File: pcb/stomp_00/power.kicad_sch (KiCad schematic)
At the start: 10 parts, among them J17 9V_Power_Input, U11 AP7333-33SRG, U8 XL1509-5.0

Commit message: came back to the project
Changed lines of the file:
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@@
+    (effects (font (size 1.27 1.27)) (justify left top))
+  )
+  (text_box "9V DC input goes to 5V via XL1509-5.0 switching regulator. AP7333 (or maybe AP7313, lower noise, used in Teensy audio adaptor schematic) provides clean 3.3V to SGTL5000."
+    (at 69.85 13.97 0) (size 60.96 30.48)
+    (stroke (width 0) (type default))
+    (fill (type none))
     (effects (font (size 1.27 1.27)) (justify left top))
   )

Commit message: seeing whether everything will fit...
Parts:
- J17: footprint Connector_BarrelJack:BarrelJack_Horizontal -> Connector_PinHeader_2.54mm:PinHeader_1x03_P2.54mm_Vertical
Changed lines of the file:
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@@
       (effects (font (size 1.27 1.27)))
     )
-    (property "Footprint" "Connector_BarrelJack:BarrelJack_Horizontal" (at 48.26 34.544 0)
+    (property "Footprint" "Connector_PinHeader_2.54mm:PinHeader_1x03_P2.54mm_Vertical" (at 48.26 34.544 0)
       (effects (font (size 1.27 1.27)) hide)
     )

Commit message: pcb...
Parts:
- removed C5, C8: 1uF, Capacitor_SMD:C_0603_1608Metric, symbol Device:C
- removed U11: AP7333-33SRG, Package_TO_SOT_SMD:SOT-23, symbol Regulator_Linear:SPX2920M3-3.3_SOT223
- C27: value 180uF 35V -> 470uF 25V
- L1: value 68uH/2A -> 22uH/2A
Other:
- note removed: "Voltage regulator for DAC, provides low-noise signal. AP7333-33SRG, as used by Pimoroni. Cheap and available on JLCPCB. Possible alternative is MIC5219-3.3YM5."

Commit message: tweaking layout, issue with usb socket placement
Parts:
- C27: footprint Capacitor_THT:CP_Radial_D8.0mm_P3.50mm -> Capacitor_THT:CP_Radial_D10.0mm_P5.00mm
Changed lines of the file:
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@@
       (effects (font (size 1.27 1.27)) (justify left))
     )
-    (property "Footprint" "Capacitor_THT:CP_Radial_D8.0mm_P3.50mm" (at 103.378 63.246 0)
+    (property "Footprint" "Capacitor_THT:CP_Radial_D10.0mm_P5.00mm" (at 103.378 63.246 0)
       (effects (font (size 1.27 1.27)) hide)
     )

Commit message: 9v power stuff
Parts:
- removed J17: 9V_Power_Input, Connector_PinHeader_2.54mm:PinHeader_1x03_P2.54mm_Vertical, symbol Connector:Barrel_Jack_Switch
- added J8: Barrel_Jack, symbol Connector:Barrel_Jack
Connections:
- net +9V: now also J8.1
- net GND: now also J8.2
- no-connect marks 1 -> 0
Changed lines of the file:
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@@
   (junction (at 40.513 59.436) (diameter 0) (color 0 0 0 0)
   )
-  (no_connect (at 54.61 35.56))
   (wire (pts (xy 40.513 59.436) (xy 48.133 59.436))
     (stroke (width 0) (type default))
@@
     (fill (type none))
     (effects (font (size 1.27 1.27)) (justify left top))
-  )
-  (symbol (lib_id "Connector:Barrel_Jack_Switch") (at 46.99 35.56 0) (mirror x) (unit 1)
-    (in_bom yes) (on_board yes) (dnp no)
-    (property "Reference" "J17" (at 46.99 42.3799 0)
-      (effects (font (size 1.27 1.27)))
-    )
-    (property "Value" "9V_Power_Input" (at 46.99 40.4589 0)
-      (effects (font (size 1.27 1.27)))
-    )
-    (property "Footprint" "Connector_PinHeader_2.54mm:PinHeader_1x03_P2.54mm_Vertical" (at 48.26 34.544 0)
-      (effects (font (size 1.27 1.27)) hide)
-    )
-    (property "Datasheet" "~" (at 48.26 34.544 0)
-      (effects (font (size 1.27 1.27)) hide)
-    )
-    (pin "1")
-    (pin "2")
-    (pin "3")
-    (instances
-      (project "dk2_00"
-        (path "/87a59a99-d509-467e-85da-26d34072acb7/be1ddc4d-f499-4b75-b4b5-b626a320d90d"
-          (reference "J17") (unit 1)
-        )
-      )
-      (project "stomp_00"
-        (path "/8f4a2eb0-078b-46cb-b534-a4acd11d130e"
-          (reference "J4") (unit 1)
-        )
-        (path "/8f4a2eb0-078b-46cb-b534-a4acd11d130e/72df8ca6-692f-47f3-a8bd-ce94f6cd776a"
-          (reference "J1") (unit 1)
-        )
-        (path "/8f4a2eb0-078b-46cb-b534-a4acd11d130e/9942492d-ba8b-45b2-b427-7fe14bedb7e0"
-          (reference "J4") (unit 1)
-        )
-      )
-    )
   )
   (symbol (lib_id "Regulator_Switching:XL1509-5.0") (at 68.453 61.976 0) (unit 1)
@@
         )
       )
+    )
+  )
+  (symbol (lib_id "Connector:Barrel_Jack") (at 46.99 35.56 0) (unit 1)
+    (in_bom yes) (on_board yes) (dnp no) (fields_autoplaced)
+    (property "Reference" "J8" (at 46.99 28.7401 0)
+      (effects (font (size 1.27 1.27)))
+    )
+    (property "Value" "Barrel_Jack" (at 46.99 30.6611 0)
+      (effects (font (size 1.27 1.27)))
+    )
+    (property "Footprint" "" (at 48.26 36.576 0)
+      (effects (font (size 1.27 1.27)) hide)
+    )
+    (property "Datasheet" "~" (at 48.26 36.576 0)
+      (effects (font (size 1.27 1.27)) hide)
+    )
+    (pin "1")
+    (pin "2")
+    (instances
+      (project "stomp_00"
+        (path "/8f4a2eb0-078b-46cb-b534-a4acd11d130e/72df8ca6-692f-47f3-a8bd-ce94f6cd776a"
+          (reference "J8") (unit 1)
+        )
+      )

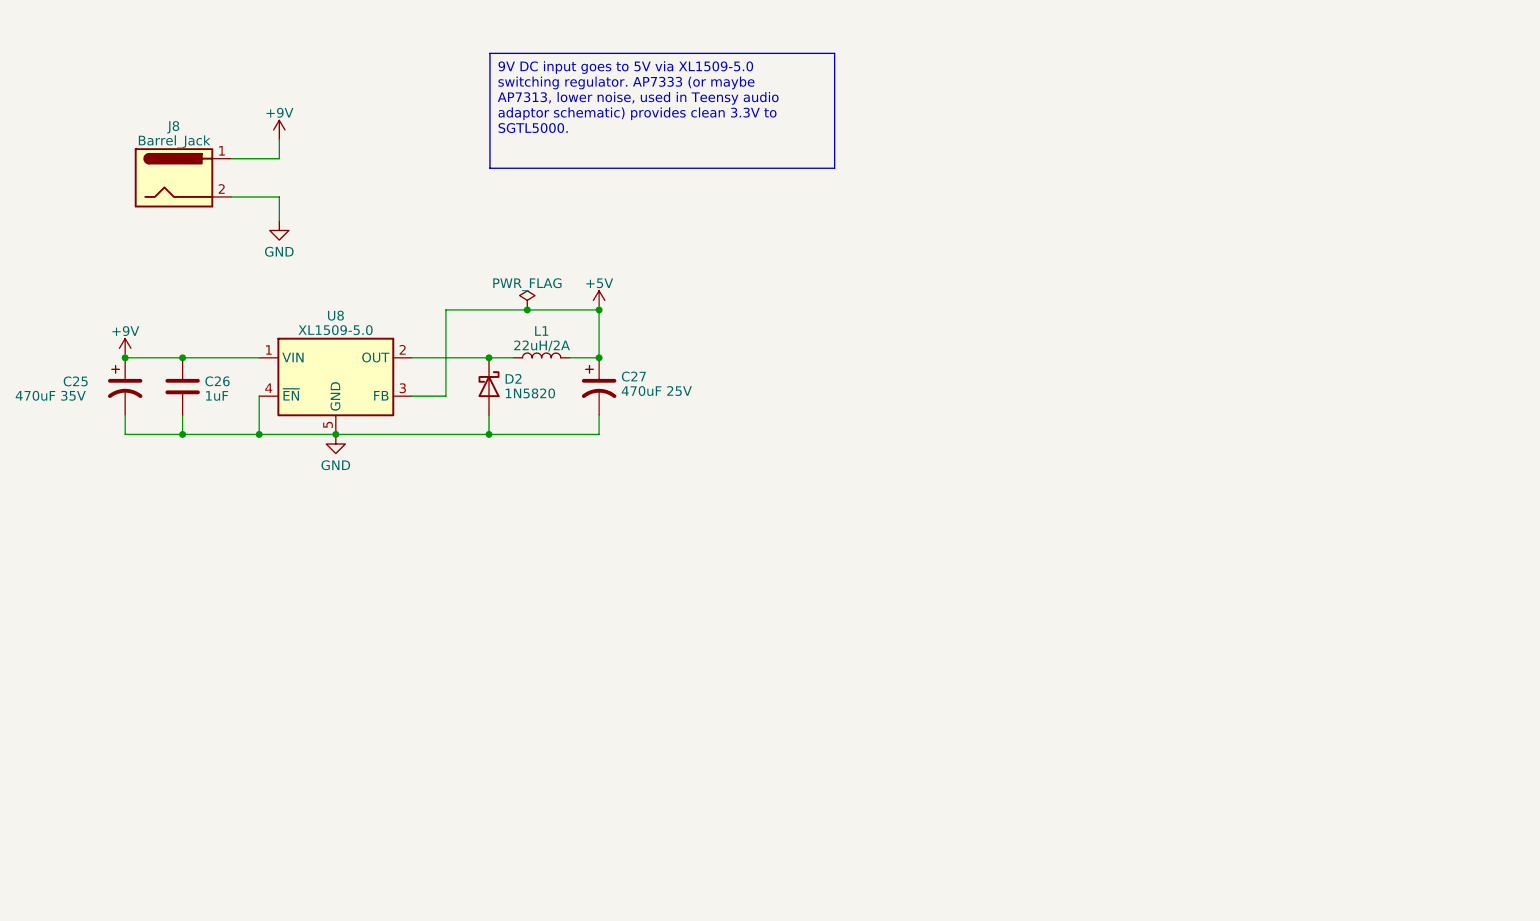
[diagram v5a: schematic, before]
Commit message: changed voltage regulator
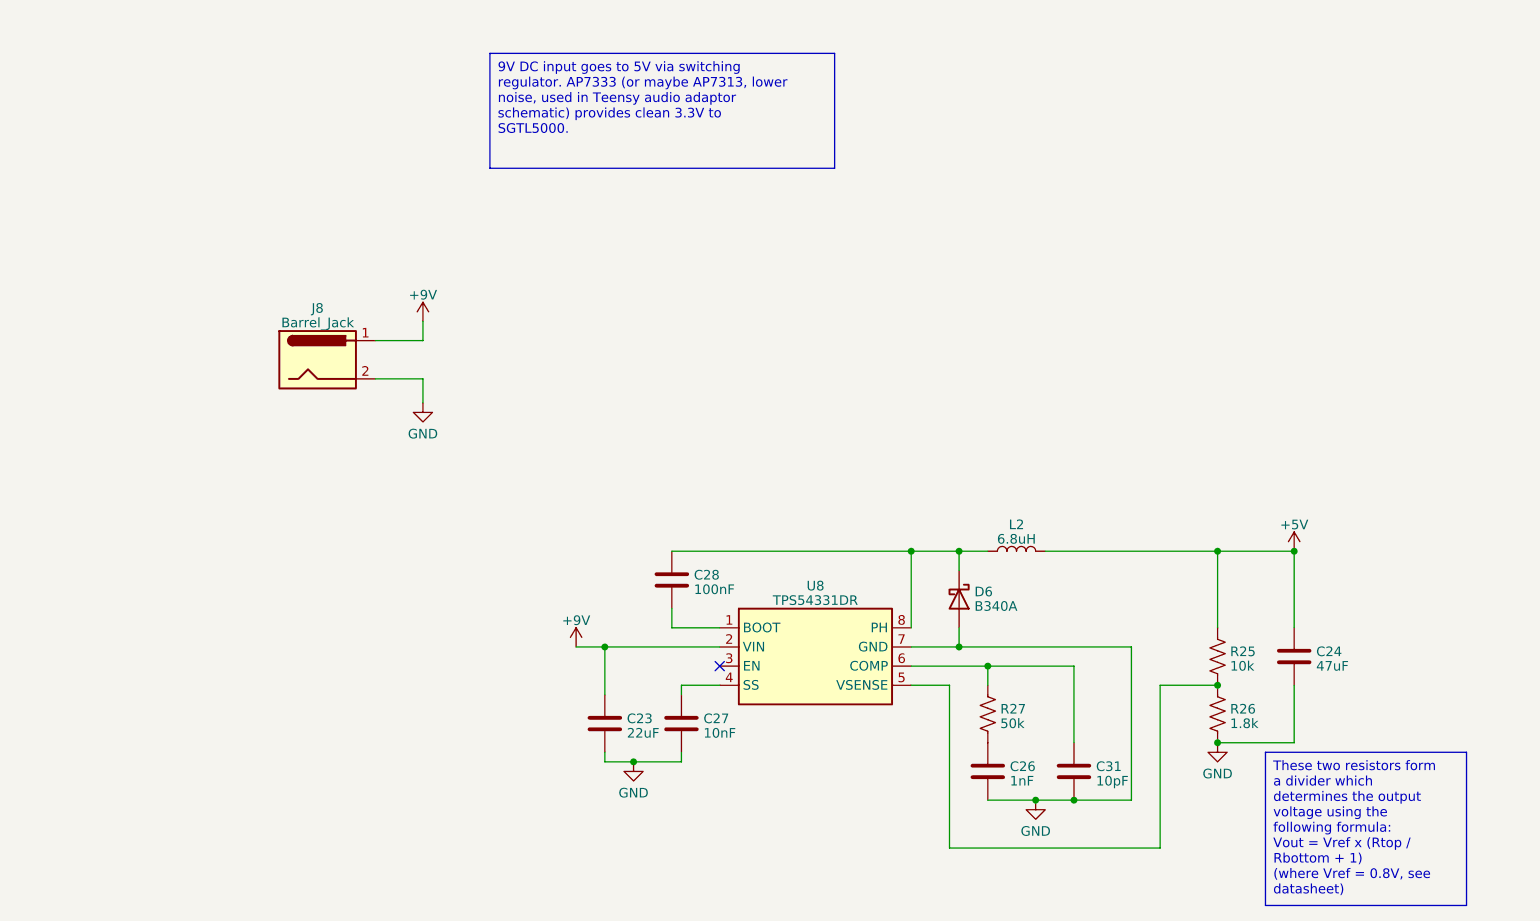
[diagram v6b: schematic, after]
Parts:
- removed C25: 470uF 35V, Capacitor_THT:CP_Radial_D10.0mm_P5.00mm, symbol Device:C_Polarized_US
- removed C27: 470uF 25V, Capacitor_THT:CP_Radial_D10.0mm_P5.00mm, symbol Device:C_Polarized_US
- removed D2: 1N5820, Diode_THT:D_DO-201AD_P15.24mm_Horizontal, symbol Diode:1N5820
- removed L1: 22uH/2A, Inductor_THT:L_Radial_D7.0mm_P3.00mm, symbol Device:L
- removed U8: XL1509-5.0, Package_SO:SOIC-8_3.9x4.9mm_P1.27mm, symbol Regulator_Switching:XL1509-5.0
- added C23: 22uF, Capacitor_SMD:C_0805_2012Metric, symbol Device:C
- added C24: 47uF, Capacitor_SMD:C_1210_3225Metric, symbol Device:C
- added C27: 10nF, Capacitor_SMD:C_0603_1608Metric, symbol Device:C
- added C28: 100nF, Capacitor_SMD:C_0603_1608Metric, symbol Device:C
- added C31: 10pF, Capacitor_SMD:C_0603_1608Metric, symbol Device:C
- added D6: B340A, Diode_SMD:D_SMA, symbol Diode:B340
- added L2: 6.8uH, Inductor_SMD:L_Changjiang_FNR4020S, symbol Device:L
- added R25: 10k, Resistor_SMD:R_0603_1608Metric, symbol Device:R_US
- added R26: 1.8k, Resistor_SMD:R_0603_1608Metric, symbol Device:R_US
- added R27: 50k, Resistor_SMD:R_0603_1608Metric, symbol Device:R_US
- added U8: TPS54331DR, Package_SO:SOIC-8_3.9x4.9mm_P1.27mm, symbol stomp:TPS54331DR
- C26: value 1uF -> 1nF
- J8: footprint (none) -> Connector_PinHeader_2.54mm:PinHeader_1x02_P2.54mm_Vertical
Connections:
- net +5V: now also C24.1, L2.2, R25.1
- net +9V: now also C23.1, U8.2 (VIN); no longer C26.1
- net GND: now also C23.2, C24.2, C27.2, C31.2, D6.2 (A), R26.2, U8.7 (GND)
- new net: R25.2, R26.1, U8.5 (VSENSE)
- new net: C26.1, R27.2
- new net: C31.1, R27.1, U8.6 (COMP)
- new net: C28.1, D6.1 (K), L2.1, U8.8 (PH)
- new net: C28.2, U8.1 (BOOT)
- new net: C27.1, U8.4 (SS)
- no-connect marks 0 -> 1
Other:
- moved on the sheet: J8

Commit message: not much
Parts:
- renumbered C23 to C1, C28 to C2, C27 to C3, C26 to C4, C31 to C5, C24 to C6, D6 to D1, J8 to J11, L2 to L1, R27 to R1, R25 to R2, R26 to R3, U8 to U2
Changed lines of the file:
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@@
   (symbol (lib_id "Device:R_US") (at 185.42 106.68 0) (unit 1)
     (in_bom yes) (on_board yes) (dnp no) (fields_autoplaced)
-    (property "Reference" "R26" (at 187.071 106.0363 0)
+    (property "Reference" "R3" (at 187.071 106.0363 0)
       (effects (font (size 1.27 1.27)) (justify left))
     )
@@
       (project "stomp_00"
         (path "/8f4a2eb0-078b-46cb-b534-a4acd11d130e/72df8ca6-692f-47f3-a8bd-ce94f6cd776a"
-          (reference "R26") (unit 1)
+          (reference "R3") (unit 1)
         )
       )
@@
         )
         (path "/8f4a2eb0-078b-46cb-b534-a4acd11d130e/72df8ca6-692f-47f3-a8bd-ce94f6cd776a"
-          (reference "#PWR041") (unit 1)
+          (reference "#PWR08") (unit 1)
         )
         (path "/8f4a2eb0-078b-46cb-b534-a4acd11d130e/9942492d-ba8b-45b2-b427-7fe14bedb7e0"
@@
   (symbol (lib_id "Connector:Barrel_Jack") (at 66.04 59.69 0) (unit 1)
     (in_bom yes) (on_board yes) (dnp no) (fields_autoplaced)
-    (property "Reference" "J8" (at 66.04 52.8701 0)
+    (property "Reference" "J11" (at 66.04 52.8701 0)
       (effects (font (size 1.27 1.27)))
     )
@@
       (project "stomp_00"
         (path "/8f4a2eb0-078b-46cb-b534-a4acd11d130e/72df8ca6-692f-47f3-a8bd-ce94f6cd776a"
-          (reference "J8") (unit 1)
+          (reference "J11") (unit 1)
         )
       )
@@
   (symbol (lib_id "Device:C") (at 154.94 114.3 0) (unit 1)
     (in_bom yes) (on_board yes) (dnp no) (fields_autoplaced)
-    (property "Reference" "C26" (at 157.861 113.6563 0)
+    (property "Reference" "C4" (at 157.861 113.6563 0)
       (effects (font (size 1.27 1.27)) (justify left))
     )
@@
       (project "stomp_00"
         (path "/8f4a2eb0-078b-46cb-b534-a4acd11d130e/72df8ca6-692f-47f3-a8bd-ce94f6cd776a"
-          (reference "C26") (unit 1)
+          (reference "C4") (unit 1)
         )
       )
@@
   (symbol (lib_id "Device:C") (at 166.37 114.3 0) (unit 1)
     (in_bom yes) (on_board yes) (dnp no) (fields_autoplaced)
-    (property "Reference" "C31" (at 169.291 113.6563 0)
+    (property "Reference" "C5" (at 169.291 113.6563 0)
       (effects (font (size 1.27 1.27)) (justify left))
     )
@@
       (project "stomp_00"
         (path "/8f4a2eb0-078b-46cb-b534-a4acd11d130e/72df8ca6-692f-47f3-a8bd-ce94f6cd776a"
-          (reference "C31") (unit 1)
+          (reference "C5") (unit 1)
         )
       )
@@
   (symbol (lib_id "Device:R_US") (at 154.94 106.68 0) (unit 1)
     (in_bom yes) (on_board yes) (dnp no) (fields_autoplaced)
-    (property "Reference" "R27" (at 156.591 106.0363 0)
+    (property "Reference" "R1" (at 156.591 106.0363 0)
       (effects (font (size 1.27 1.27)) (justify left))
     )
@@
       (project "stomp_00"
         (path "/8f4a2eb0-078b-46cb-b534-a4acd11d130e/72df8ca6-692f-47f3-a8bd-ce94f6cd776a"
-          (reference "R27") (unit 1)
+          (reference "R1") (unit 1)
         )
       )
@@
   (symbol (lib_id "Device:R_US") (at 185.42 99.06 0) (unit 1)
     (in_bom yes) (on_board yes) (dnp no) (fields_autoplaced)
-    (property "Reference" "R25" (at 187.071 98.4163 0)
+    (property "Reference" "R2" (at 187.071 98.4163 0)
       (effects (font (size 1.27 1.27)) (justify left))
     )
@@
       (project "stomp_00"
         (path "/8f4a2eb0-078b-46cb-b534-a4acd11d130e/72df8ca6-692f-47f3-a8bd-ce94f6cd776a"
-          (reference "R25") (unit 1)
+          (reference "R2") (unit 1)
         )
       )
@@
         )
         (path "/8f4a2eb0-078b-46cb-b534-a4acd11d130e/72df8ca6-692f-47f3-a8bd-ce94f6cd776a"
-          (reference "#PWR039") (unit 1)
+          (reference "#PWR07") (unit 1)
         )
         (path "/8f4a2eb0-078b-46cb-b534-a4acd11d130e/9942492d-ba8b-45b2-b427-7fe14bedb7e0"
@@
   (symbol (lib_id "Device:L") (at 158.75 85.09 90) (unit 1)
     (in_bom yes) (on_board yes) (dnp no) (fields_autoplaced)
-    (property "Reference" "L2" (at 158.75 81.5747 90)
+    (property "Reference" "L1" (at 158.75 81.5747 90)
       (effects (font (size 1.27 1.27)))
     )
@@
       (project "stomp_00"
         (path "/8f4a2eb0-078b-46cb-b534-a4acd11d130e/72df8ca6-692f-47f3-a8bd-ce94f6cd776a"
-          (reference "L2") (unit 1)
+          (reference "L1") (unit 1)
         )
       )
@@
   (symbol (lib_id "Device:C") (at 113.03 88.9 0) (unit 1)
     (in_bom yes) (on_board yes) (dnp no) (fields_autoplaced)
-    (property "Reference" "C28" (at 115.951 88.2563 0)
+    (property "Reference" "C2" (at 115.951 88.2563 0)
       (effects (font (size 1.27 1.27)) (justify left))
     )
@@
       (project "stomp_00"
         (path "/8f4a2eb0-078b-46cb-b534-a4acd11d130e/72df8ca6-692f-47f3-a8bd-ce94f6cd776a"
-          (reference "C28") (unit 1)
+          (reference "C2") (unit 1)
         )
       )
@@
   (symbol (lib_id "Device:C") (at 195.58 99.06 0) (unit 1)
     (in_bom yes) (on_board yes) (dnp no) (fields_autoplaced)
-    (property "Reference" "C24" (at 198.501 98.4163 0)
+    (property "Reference" "C6" (at 198.501 98.4163 0)
       (effects (font (size 1.27 1.27)) (justify left))
     )
@@
       (project "stomp_00"
         (path "/8f4a2eb0-078b-46cb-b534-a4acd11d130e/72df8ca6-692f-47f3-a8bd-ce94f6cd776a"
-          (reference "C24") (unit 1)
+          (reference "C6") (unit 1)
         )
       )
@@
   (symbol (lib_id "stomp:TPS54331DR") (at 132.08 100.33 0) (unit 1)
     (in_bom yes) (on_board yes) (dnp no) (fields_autoplaced)
-    (property "Reference" "U8" (at 132.08 89.7001 0)
+    (property "Reference" "U2" (at 132.08 89.7001 0)
       (effects (font (size 1.27 1.27)))
     )
@@
       (project "stomp_00"
         (path "/8f4a2eb0-078b-46cb-b534-a4acd11d130e/72df8ca6-692f-47f3-a8bd-ce94f6cd776a"
-          (reference "U8") (unit 1)
+          (reference "U2") (unit 1)
         )
       )
@@
         )
         (path "/8f4a2eb0-078b-46cb-b534-a4acd11d130e/72df8ca6-692f-47f3-a8bd-ce94f6cd776a"
-          (reference "#PWR06") (unit 1)
+          (reference "#PWR05") (unit 1)
         )
         (path "/8f4a2eb0-078b-46cb-b534-a4acd11d130e/9942492d-ba8b-45b2-b427-7fe14bedb7e0"
@@
   (symbol (lib_id "Device:C") (at 114.3 107.95 0) (unit 1)
     (in_bom yes) (on_board yes) (dnp no) (fields_autoplaced)
-    (property "Reference" "C27" (at 117.221 107.3063 0)
+    (property "Reference" "C3" (at 117.221 107.3063 0)
       (effects (font (size 1.27 1.27)) (justify left))
     )
@@
       (project "stomp_00"
         (path "/8f4a2eb0-078b-46cb-b534-a4acd11d130e/72df8ca6-692f-47f3-a8bd-ce94f6cd776a"
-          (reference "C27") (unit 1)
+          (reference "C3") (unit 1)
         )
       )
@@
         )
         (path "/8f4a2eb0-078b-46cb-b534-a4acd11d130e/72df8ca6-692f-47f3-a8bd-ce94f6cd776a"
-          (reference "#PWR05") (unit 1)
+          (reference "#PWR04") (unit 1)
         )
         (path "/8f4a2eb0-078b-46cb-b534-a4acd11d130e/9942492d-ba8b-45b2-b427-7fe14bedb7e0"
@@
         )
         (path "/8f4a2eb0-078b-46cb-b534-a4acd11d130e/72df8ca6-692f-47f3-a8bd-ce94f6cd776a"
-          (reference "#PWR042") (unit 1)
+          (reference "#PWR09") (unit 1)
         )
         (path "/8f4a2eb0-078b-46cb-b534-a4acd11d130e/9942492d-ba8b-45b2-b427-7fe14bedb7e0"
@@
         )
         (path "/8f4a2eb0-078b-46cb-b534-a4acd11d130e/72df8ca6-692f-47f3-a8bd-ce94f6cd776a"
-          (reference "#PWR037") (unit 1)
+          (reference "#PWR010") (unit 1)
         )
         (path "/8f4a2eb0-078b-46cb-b534-a4acd11d130e/9942492d-ba8b-45b2-b427-7fe14bedb7e0"
@@
   (symbol (lib_id "Diode:B340") (at 151.13 91.44 270) (unit 1)
     (in_bom yes) (on_board yes) (dnp no) (fields_autoplaced)
-    (property "Reference" "D6" (at 153.162 90.4788 90)
+    (property "Reference" "D1" (at 153.162 90.4788 90)
       (effects (font (size 1.27 1.27)) (justify left))
     )
@@
       (project "stomp_00"
         (path "/8f4a2eb0-078b-46cb-b534-a4acd11d130e/72df8ca6-692f-47f3-a8bd-ce94f6cd776a"
-          (reference "D6") (unit 1)
+          (reference "D1") (unit 1)
         )
       )
@@
         )
         (path "/8f4a2eb0-078b-46cb-b534-a4acd11d130e/72df8ca6-692f-47f3-a8bd-ce94f6cd776a"
-          (reference "#PWR015") (unit 1)
+          (reference "#PWR06") (unit 1)
         )
         (path "/8f4a2eb0-078b-46cb-b534-a4acd11d130e/9942492d-ba8b-45b2-b427-7fe14bedb7e0"
@@
   (symbol (lib_id "Device:C") (at 104.14 107.95 0) (unit 1)
     (in_bom yes) (on_board yes) (dnp no) (fields_autoplaced)
-    (property "Reference" "C23" (at 107.061 107.3063 0)
+    (property "Reference" "C1" (at 107.061 107.3063 0)
       (effects (font (size 1.27 1.27)) (justify left))
     )
@@
       (project "stomp_00"
         (path "/8f4a2eb0-078b-46cb-b534-a4acd11d130e/72df8ca6-692f-47f3-a8bd-ce94f6cd776a"
-          (reference "C23") (unit 1)
-        )
-      )
+          (reference "C1") (unit 1)
+        )
+      )
